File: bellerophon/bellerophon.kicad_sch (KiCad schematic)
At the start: 50 parts, among them Q1 ST3413A, Q2 SPP3414S23RG, Q3 SPP3414S23RG, U1 HT7350-A, U2 BNO055, U3 MPL3115A2, U4 Teensy4.0, U5 XTSD, Y1 32.768kHz

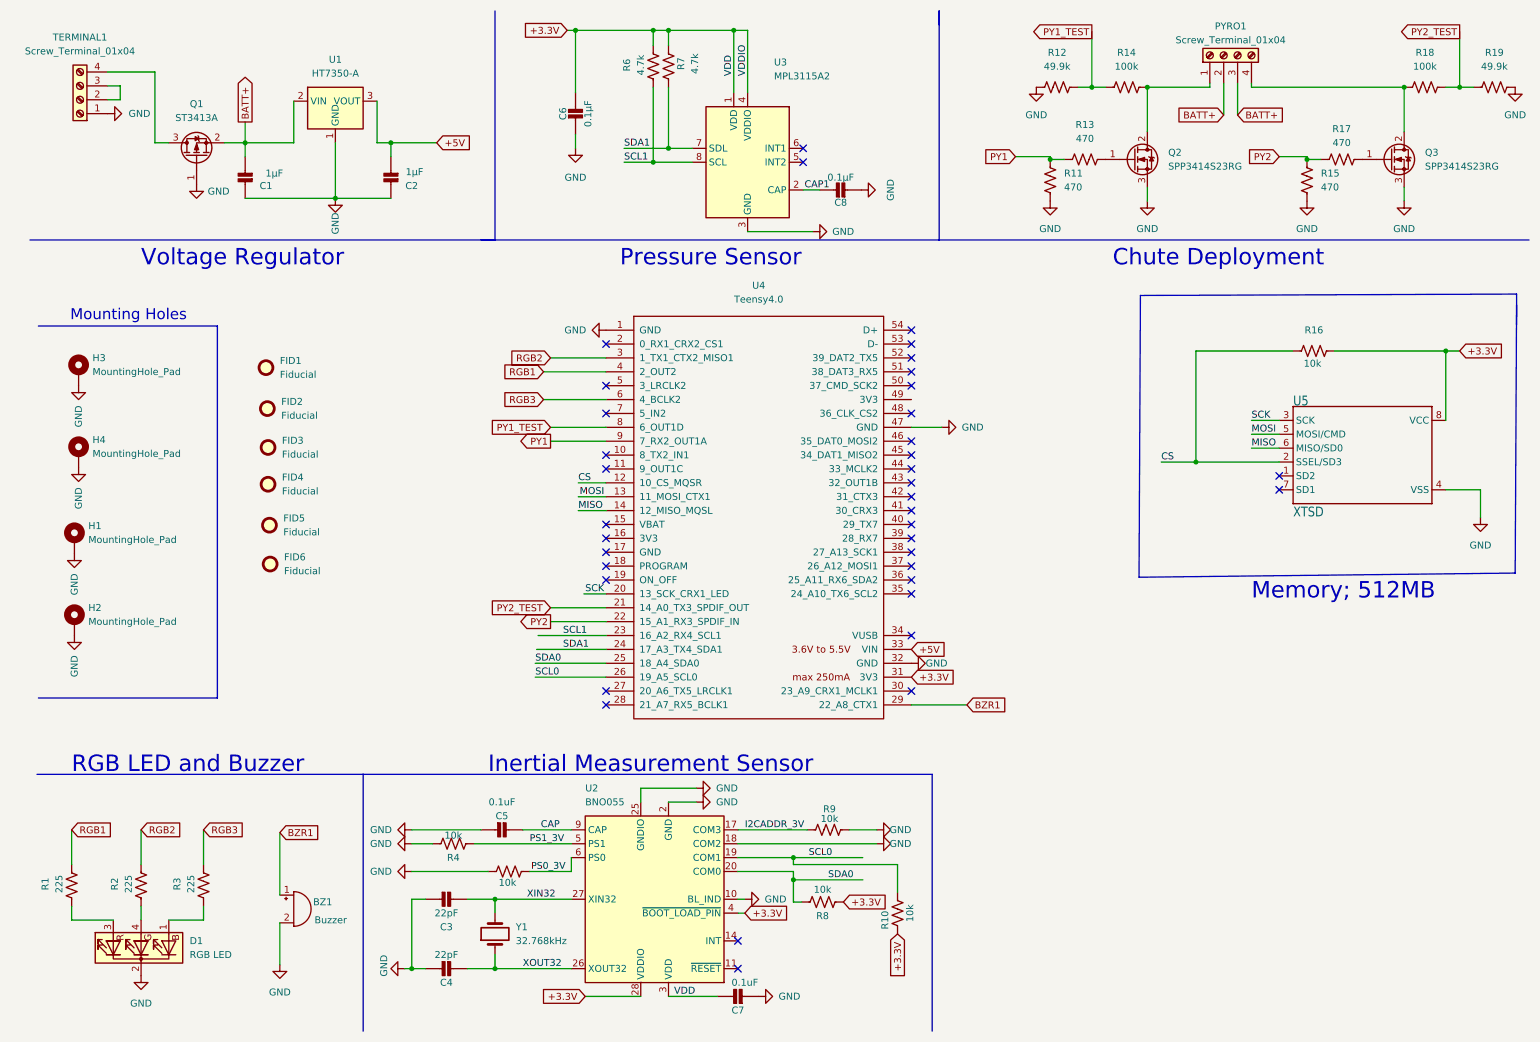
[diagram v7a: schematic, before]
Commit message: add JLC component numbers to all parts, define drill origin
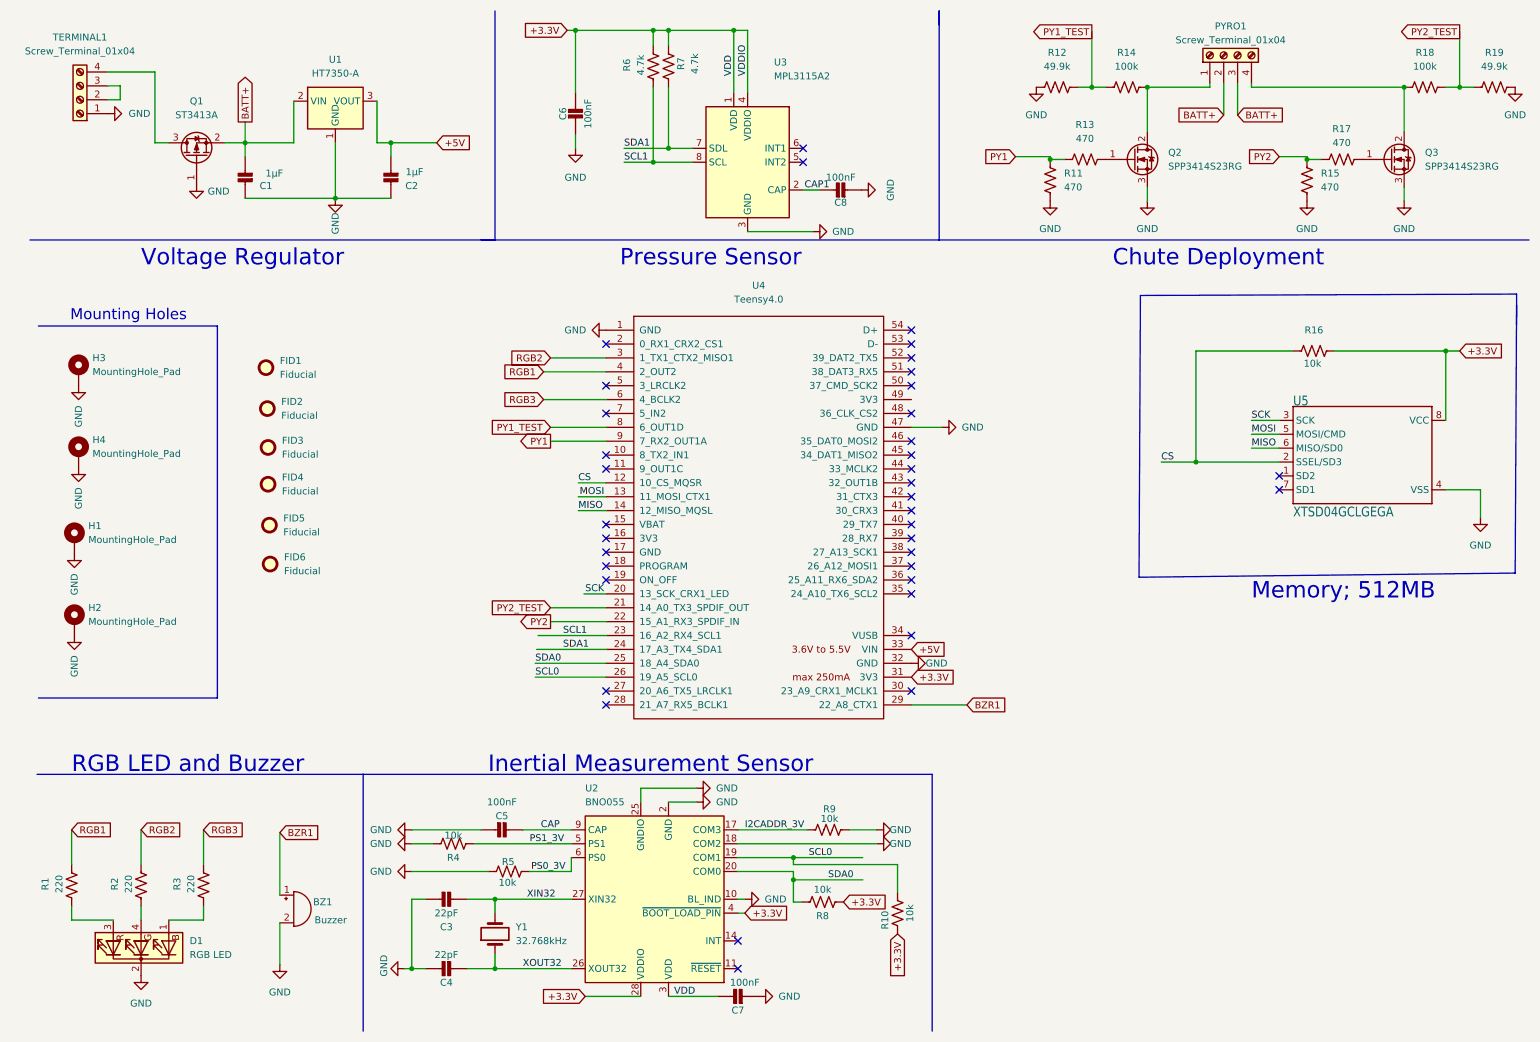
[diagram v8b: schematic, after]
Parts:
- C1, C2: LCSC (none) -> C89190
- C3, C4: LCSC (none) -> C24658
- C5, C7: value 0.1uF -> 100nF; LCSC (none) -> C286511
- C6, C8: value 0.1µF -> 100nF; LCSC (none) -> C286511
- Q1: LCSC (none) -> C710092
- Q2, Q3: LCSC (none) -> C725192
- R1, R2, R3: value 225 -> 220; LCSC (none) -> C176196
- R10, R16, R4, R5, R8, R9: footprint Resistor_SMD:R_0805_2012Metric -> Resistor_SMD:R_0805_2012Metric_Pad1.20x1.40mm_HandSolder; LCSC (none) -> C332266
- R11, R13, R15, R17: footprint Resistor_SMD:R_1206_3216Metric -> Resistor_SMD:R_1206_3216Metric_Pad1.30x1.75mm_HandSolder; LCSC (none) -> C4502
- R12, R19: footprint Resistor_SMD:R_1206_3216Metric -> Resistor_SMD:R_1206_3216Metric_Pad1.30x1.75mm_HandSolder; LCSC (none) -> C18017
- R14, R18: footprint Resistor_SMD:R_1206_3216Metric -> Resistor_SMD:R_1206_3216Metric_Pad1.30x1.75mm_HandSolder; LCSC (none) -> C17900
- R6, R7: footprint Resistor_SMD:R_0805_2012Metric -> Resistor_SMD:R_0805_2012Metric_Pad1.20x1.40mm_HandSolder; LCSC (none) -> C17673
- U1: LCSC (none) -> C7874
- U2: LCSC (none) -> C93216
- U3: LCSC (none) -> C54429
- U5: value XTSD -> XTSD04GCLGEGA; LCSC (none) -> C2759953
- Y1: LCSC (none) -> C528990
